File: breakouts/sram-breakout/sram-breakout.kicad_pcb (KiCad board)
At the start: 2 copper layers, 22.9 x 27.9 mm, 7 parts, among them J1 Conn_01x09, J2 Conn_01x09, U1 S71KL512SC0

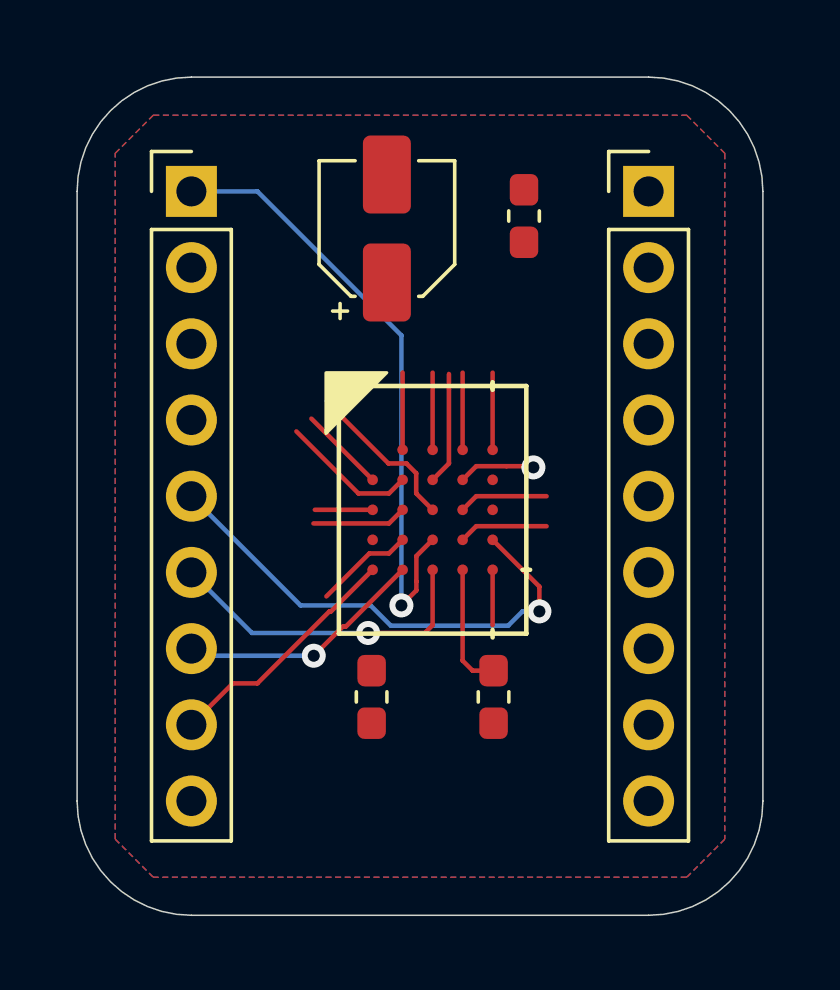
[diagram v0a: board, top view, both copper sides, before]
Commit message: Laid out the HyperRAM PSRAM breakout PCB
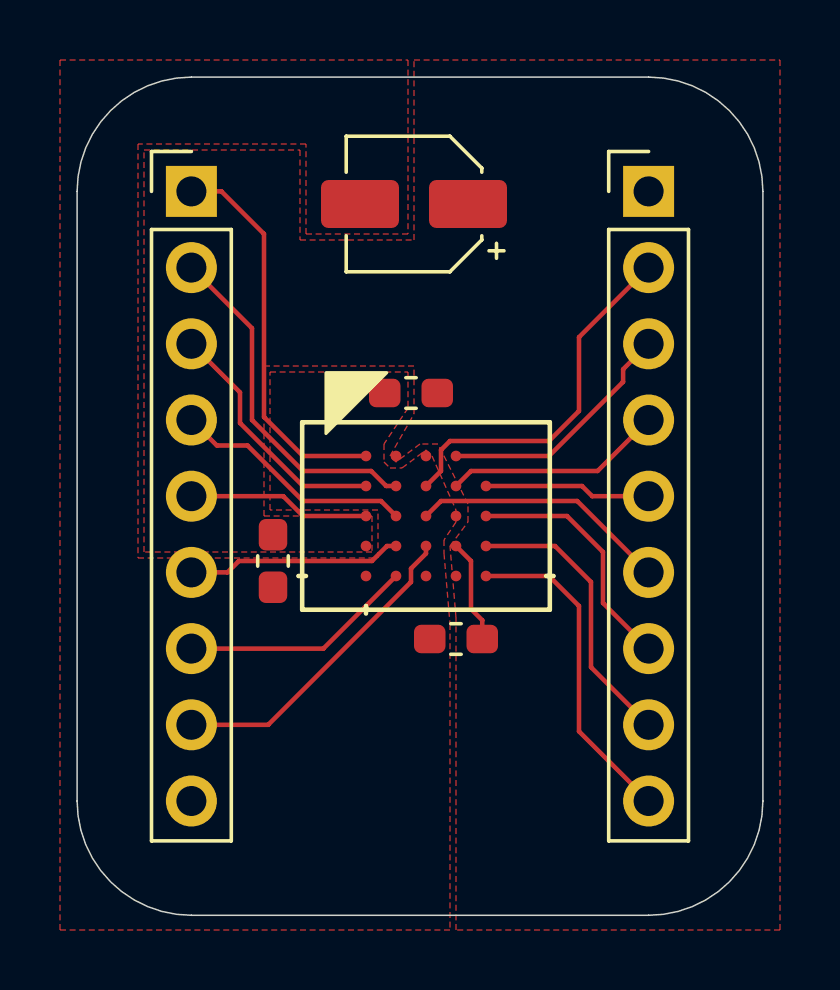
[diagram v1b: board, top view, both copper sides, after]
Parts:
- moved C1 7.00 mm to (50.5, 49.9), turned to 180 degrees
- moved C3 5.60 mm to (45.9, 55.5)
- moved C2 2.30 mm to (52.0, 58.1), turned to 180 degrees
- moved C4 1.22 mm to (50.6, 43.6), turned to 180 degrees
- moved U1 0.30 mm to (51.0, 54.0), turned to -90 degrees
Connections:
- J1 pad 1: /DQ0 -> /DQ7
- J1 pad 3: /DQ2 -> /DQ6
- J1 pad 4: /DQ3 -> /DQ0
- J1 pad 5: /DQ4 -> /DQ5
- J1 pad 6: /DQ5 -> /DQ3
- J1 pad 7: /DQ6 -> /DQ4
- J1 pad 8: /DQ7 -> /DQ2
- J2 pad 2: /CK -> /~CS1
- J2 pad 4: /RWDS -> /CK
- J2 pad 5: /~CS1 -> /~RSTO
- J2 pad 6: /~CS2 -> /RWDS
- J2 pad 7: /~INT -> /~CS2
- J2 pad 8: /~RSTO -> /~RESET
- J2 pad 9: /~RESET -> /~INT
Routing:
- net /DQ0: track 20.6 -> 8.15 mm, vias 1 -> 0
- net /~CS1: track 3.16 -> 12.3 mm
- net /DQ4: track 16.6 -> 8.16 mm, vias 1 -> 0
- net /~INT: track 2.57 -> 11.0 mm
- net /DQ1: track 3.32 -> 11.6 mm
- net /DQ2: track 2.99 -> 10.7 mm
- net GND: track 7.53 -> 0.00 mm
- net /~RESET: track 2.57 -> 9.55 mm
- net /~CS2: track 2.57 -> 8.25 mm
- net /~CK: track 2.88 -> 8.22 mm
- net /DQ7: track 8.18 -> 13.0 mm
- net /DQ5: track 10.8 -> 6.09 mm, vias 1 -> 0
- net /DQ3: track 2.99 -> 7.18 mm
- net +3V3: track 6.76 -> 3.46 mm, vias 1 -> 0
- net /RWDS: track 5.43 -> 8.61 mm
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- added copper zone on F.Cu, net +3V3
- removed copper zone on B.Cu, net +3V3
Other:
- net class Default: clearance 0.2 -> 0.15; trace_width 0.25 -> 0.15
- rule trace_clearance: 0.2 -> 0.15

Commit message: Updating SRAM breakout board to be 0.3 inch wide
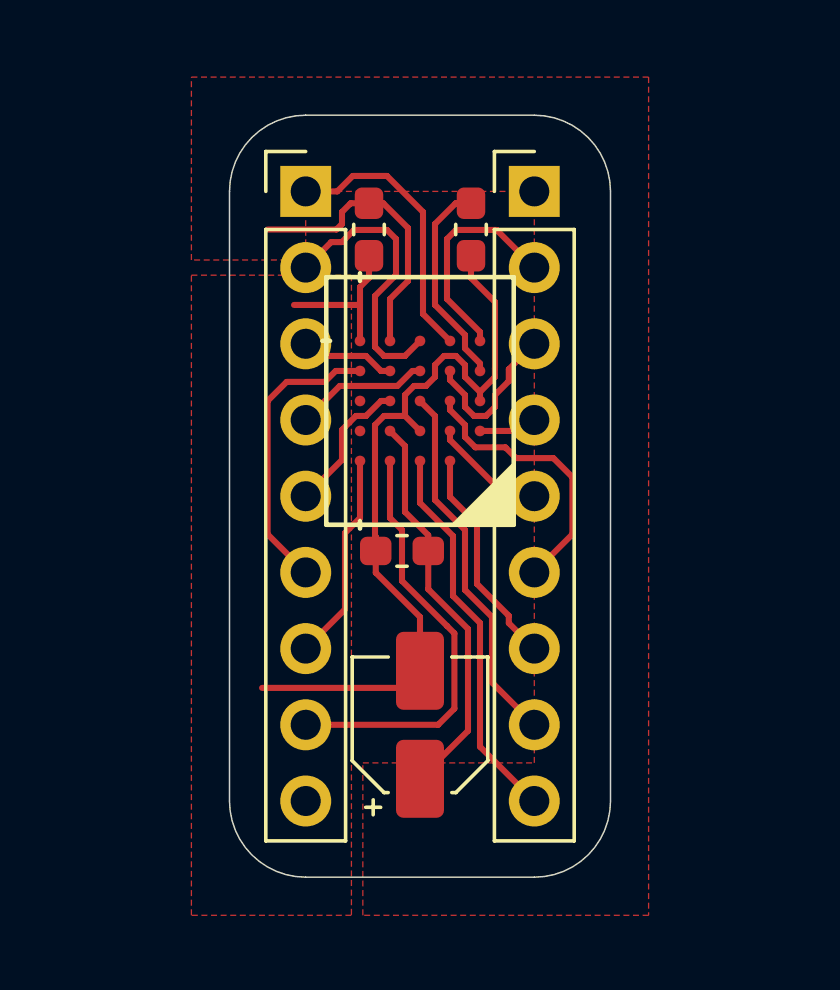
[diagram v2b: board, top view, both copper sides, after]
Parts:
- moved C4 17.4 mm to (50.8, 61.0), turned to 90 degrees
- moved C3 11.5 mm to (49.1, 44.5)
- moved C1 5.81 mm to (52.5, 44.5), turned to -90 degrees
- moved U1 3.84 mm to (50.8, 50.2), turned to 180 degrees
- moved J1 3.81 mm to (47.0, 43.2)
- moved J2 3.81 mm to (54.6, 43.2)
- moved C2 3.44 mm to (50.2, 55.2)
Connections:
- J1 pad 1: /DQ7 -> /DQ6
- J1 pad 2: /DQ1 -> /DQ5
- J1 pad 3: /DQ6 -> /DQ3
- J1 pad 5: /DQ5 -> /DQ2
- J1 pad 6: /DQ3 -> /DQ4
- J1 pad 7: /DQ4 -> /~INT
- J1 pad 8: /DQ2 -> /~RESET
- J2 pad 2: /~CS1 -> /DQ7
- J2 pad 3: /~CK -> /DQ1
- J2 pad 4: /CK -> /~CK
- J2 pad 5: /~RSTO -> /CK
- J2 pad 6: /RWDS -> /~CS1
- J2 pad 7: /~CS2 -> /~RSTO
- J2 pad 8: /~RESET -> /RWDS
- J2 pad 9: /~INT -> /~CS2
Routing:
- net GND: track 0.00 -> 31.2 mm
- net +3V3: track 3.46 -> 30.0 mm
- net /DQ1: track 11.6 -> 5.30 mm
- net /~CK: track 8.22 -> 1.96 mm
- net /DQ2: track 10.7 -> 4.71 mm
- net /DQ7: track 13.0 -> 7.41 mm
- net /~RESET: track 9.55 -> 14.3 mm
- net /~CS2: track 8.25 -> 12.9 mm
- net /DQ3: track 7.18 -> 3.18 mm
- net /~INT: track 11.0 -> 7.00 mm
- net /RWDS: track 8.61 -> 12.4 mm
- net /DQ0: track 8.15 -> 4.49 mm
- net /CK: track 7.33 -> 3.91 mm
- net /DQ5: track 6.09 -> 9.38 mm
- net /~CS1: track 12.3 -> 9.24 mm
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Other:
- board size 22.9 x 27.9 mm -> 12.7 x 25.4 mm
- net class Default: clearance 0.15 -> 0.1524; trace_width 0.15 -> 0.1524
- rule trace_clearance: 0.15 -> 0.1524
- rule trace_min: 0.1 -> 0.1524
